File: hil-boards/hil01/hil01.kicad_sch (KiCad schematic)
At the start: 34 parts, among them J1 USB_C_Receptacle_USB2.0, J2 RJ25, J3 Conn_01x08_Male, J4 Conn_01x02_Male, J5 Conn_01x03_Male, U1 ADUM4160, U2 AMS1117-3.3, U3 CH340G, U4 MAX485E, Y1 Crystal

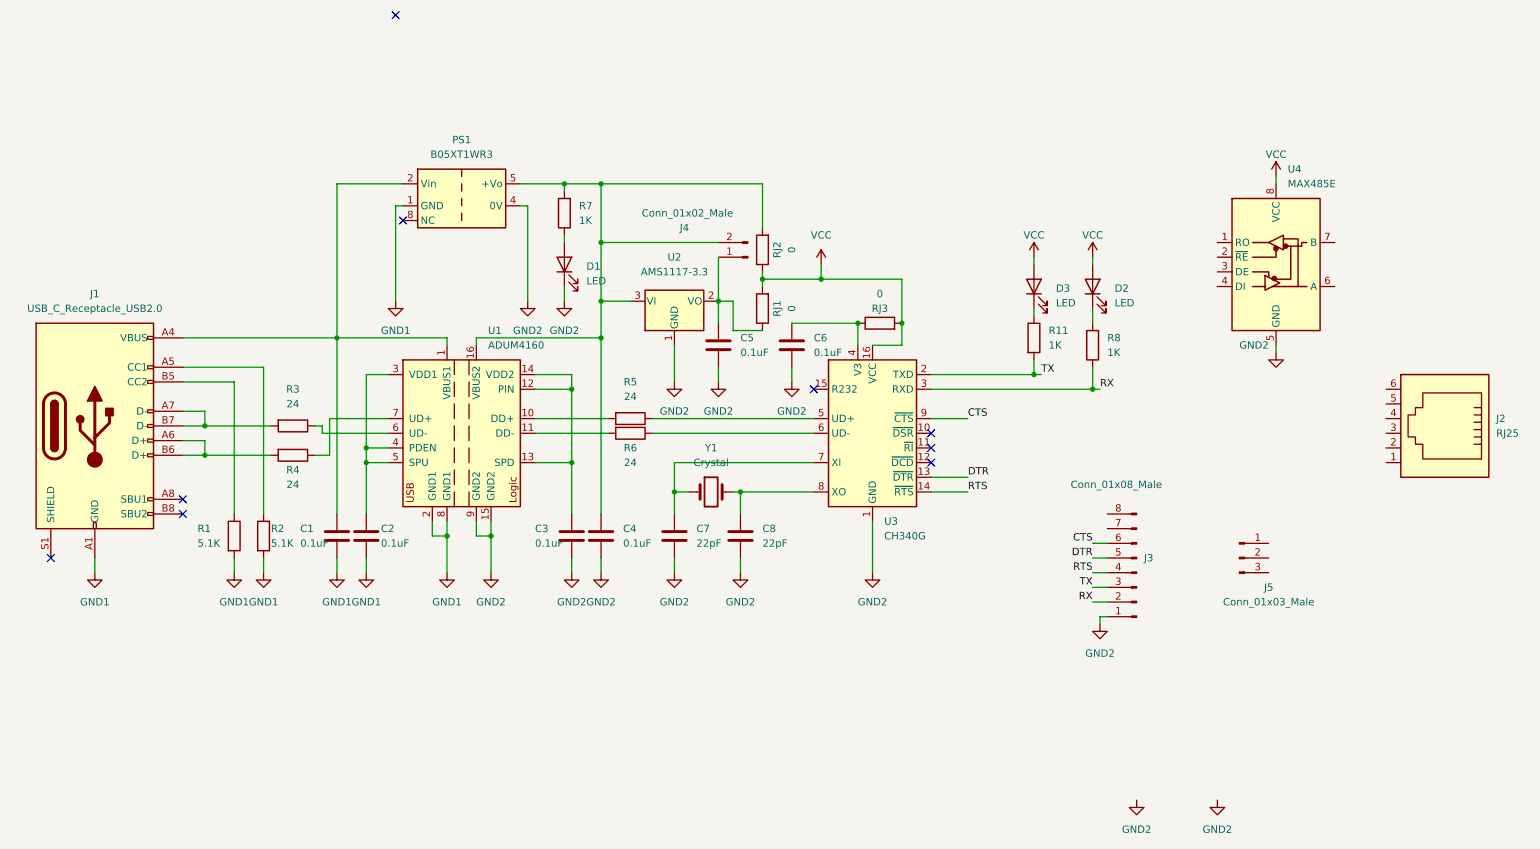
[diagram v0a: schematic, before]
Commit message: updated rs485 footprint
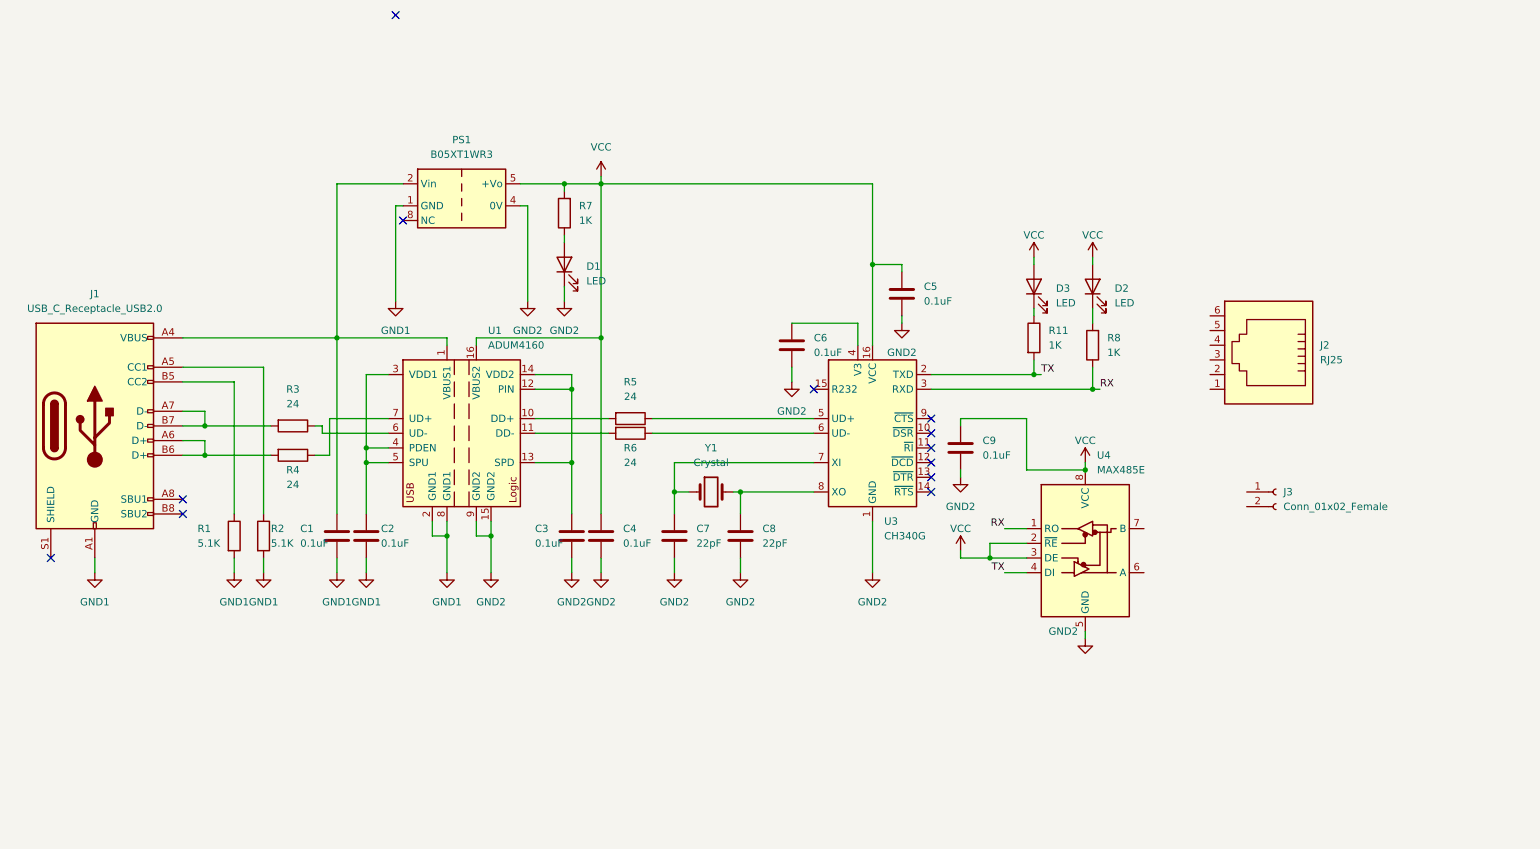
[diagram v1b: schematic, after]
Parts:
- removed J3: Conn_01x08_Male, Connector_PinHeader_2.54mm:PinHeader_1x08_P2.54mm_Vertical, symbol Connector:Conn_01x08_Male
- removed J4: Conn_01x02_Male, Connector_PinHeader_2.54mm:PinHeader_1x02_P2.54mm_Vertical, symbol Connector:Conn_01x02_Male
- removed J5: Conn_01x03_Male, Connector_PinHeader_2.54mm:PinHeader_1x03_P2.54mm_Vertical, symbol Connector:Conn_01x03_Male
- removed RJ1, RJ2, RJ3: 0, Resistor_SMD:R_0805_2012Metric_Pad1.20x1.40mm_HandSolder, symbol Device:R
- removed U2: AMS1117-3.3, Package_TO_SOT_SMD:SOT-223-3_TabPin2, symbol Regulator_Linear:AMS1117-3.3
- added C9: 0.1uF, Capacitor_SMD:C_0805_2012Metric_Pad1.18x1.45mm_HandSolder, symbol Device:C
- added J3: Conn_01x02_Female, Connector_Kefa:TerminalBlock_Kefa_1x02_P6.35mm_Horizontal, symbol Connector:Conn_01x02_Female
- U4: footprint Package_SO:SO-8_5.3x6.2mm_P1.27mm -> Package_SO:SO-8_3.9x4.9mm_P1.27mm
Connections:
- net GND2: now also C9.2
- net RX: now also U4.1 (RO)
- net TX: now also U4.4 (DI)
- net VCC: now also C4.1, C5.1, PS1.5 (+Vo), R7.2, U1.16 (VBUS2), U4.2 (~{RE}), U4.3 (DE), C9.1
- net CTS: no longer names the net of U3.9 (~{CTS})
- net DTR: no longer names the net of U3.13 (~{DTR})
- net RTS: no longer names the net of U3.14 (~{RTS})
- no-connect marks 9 -> 12
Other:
- moved on the sheet: C5, J2, U4
